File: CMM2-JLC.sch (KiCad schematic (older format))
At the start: 61 parts, among them J1 Nunchuck, J2 VGA, J3 EXTERNAL I/O, U1 STM32H743IITx, U2 MT48LC16M16A2P

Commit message: Add USB-UART, power, microSD
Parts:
- added C? (x6): 100n, Capacitor_SMD:C_0402_1005Metric, symbol Device:C
- added C? (x2): 1u, Capacitor_SMD:C_0402_1005Metric, symbol Device:C
- added C?: 4.7u, Capacitor_SMD:C_0402_1005Metric, symbol Device:C
- added C?: 10u, Capacitor_SMD:C_0603_1608Metric, symbol Device:C
- added C?: 22u, Capacitor_SMD:C_0603_1608Metric, symbol Device:C
- added J?: USB_C_Receptacle_USB2.0, symbol Connector:USB_C_Receptacle_USB2.0
- added J?: Micro_SD_Card_Det, CMM2-JLC:HOAUC_HYC77-TF09-200, symbol Connector:Micro_SD_Card_Det
- added R? (x2): 5.1k, Resistor_SMD:R_0402_1005Metric, symbol Device:R
- added R?: 4.7k, Resistor_SMD:R_0402_1005Metric, symbol Device:R
- added R?: 120R, Resistor_SMD:R_0603_1608Metric, symbol Device:R
- added R?: 10R, Resistor_SMD:R_0402_1005Metric, symbol Device:R
- added U?: SRV05-4, Package_TO_SOT_SMD:SOT-23-6, symbol Power_Protection:SRV05-4
- added U?: CP2102N-A01-GQFN28, Package_DFN_QFN:QFN-28-1EP_5x5mm_P0.5mm_EP3.35x3.35mm, symbol Interface_USB:CP2102N-A01-GQFN28
- added U?: AMS1117-3.3, Package_TO_SOT_SMD:SOT-223-3_TabPin2, symbol Regulator_Linear:AMS1117-3.3
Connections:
- net PH12 is gone; now on net GND: U1.89 (PH12)
- net +3V3: now also C?.1, C?.1, C?.1, C?.1, J?.4 (VDD), R?.1, U?.2 (VO)
- net +5V: now also C?.1, C?.1, C?.1, C?.1, J?.A4 (VBUS), J?.A9 (VBUS), J?.B4 (VBUS), J?.B9 (VBUS), U?.3 (VI), U?.5 (VP), U?.7 (REGIN), U?.8 (VBUS)
- net GND: now also C?.2, C?.2, C?.2, C?.2, C?.2, C?.2, C?.2, C?.2, C?.2, C?.2, C?.2, J?.11 (SHIELD), J?.6 (VSS), J?.9 (DET_B), J?.A1 (GND), J?.A12 (GND), J?.B1 (GND), J?.B12 (GND), J?.S1 (SHIELD), R?.1, R?.2, U?.1 (GND), U?.2 (VN), U?.29 (GND), U?.3 (GND)
- net PA11: now also U?.6 (IO4)
- net PA12: now also U?.4 (IO3)
- net PC10: now also J?.5 (CLK)
- net PC11: now also J?.7 (DAT0)
- net PC12: now also J?.3 (CMD)
- net PD2: now also J?.2 (DAT3/CD)
- net PD3: now also J?.10 (DET_A)
- net at U1.38 (VREF+): now also C?.1, R?.2
- new net: J?.A5 (CC1), R?.2
- new net: J?.B5 (CC2), R?.1
- new net: R?.2, U?.26 (TXD)
- new net: C?.1, C?.1, R?.2, U?.6 (VDD)
- new net: R?.1, U?.9 (~RSTb)
- new net PA10: R?.1
- new net PA9: U?.25 (RXD)
- new net USB_C_DM: J?.A7 (D-), J?.B7 (D-), U?.1 (IO1), U?.5 (D-)
- new net USB_C_DP: J?.A6 (D+), J?.B6 (D+), U?.3 (IO2), U?.4 (D+)
- no-connect marks 5 -> 27
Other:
- note added: "FIXME: SWD Headers"
- note added: "POWER"
- note added: "USB ESD Protection"
- note added: "USB UART"
- note added: "Write Protect\n(not present on microSD)"
- note added: "microSD"
- moved on the sheet: C1, C2, C3, C4, C5, J?

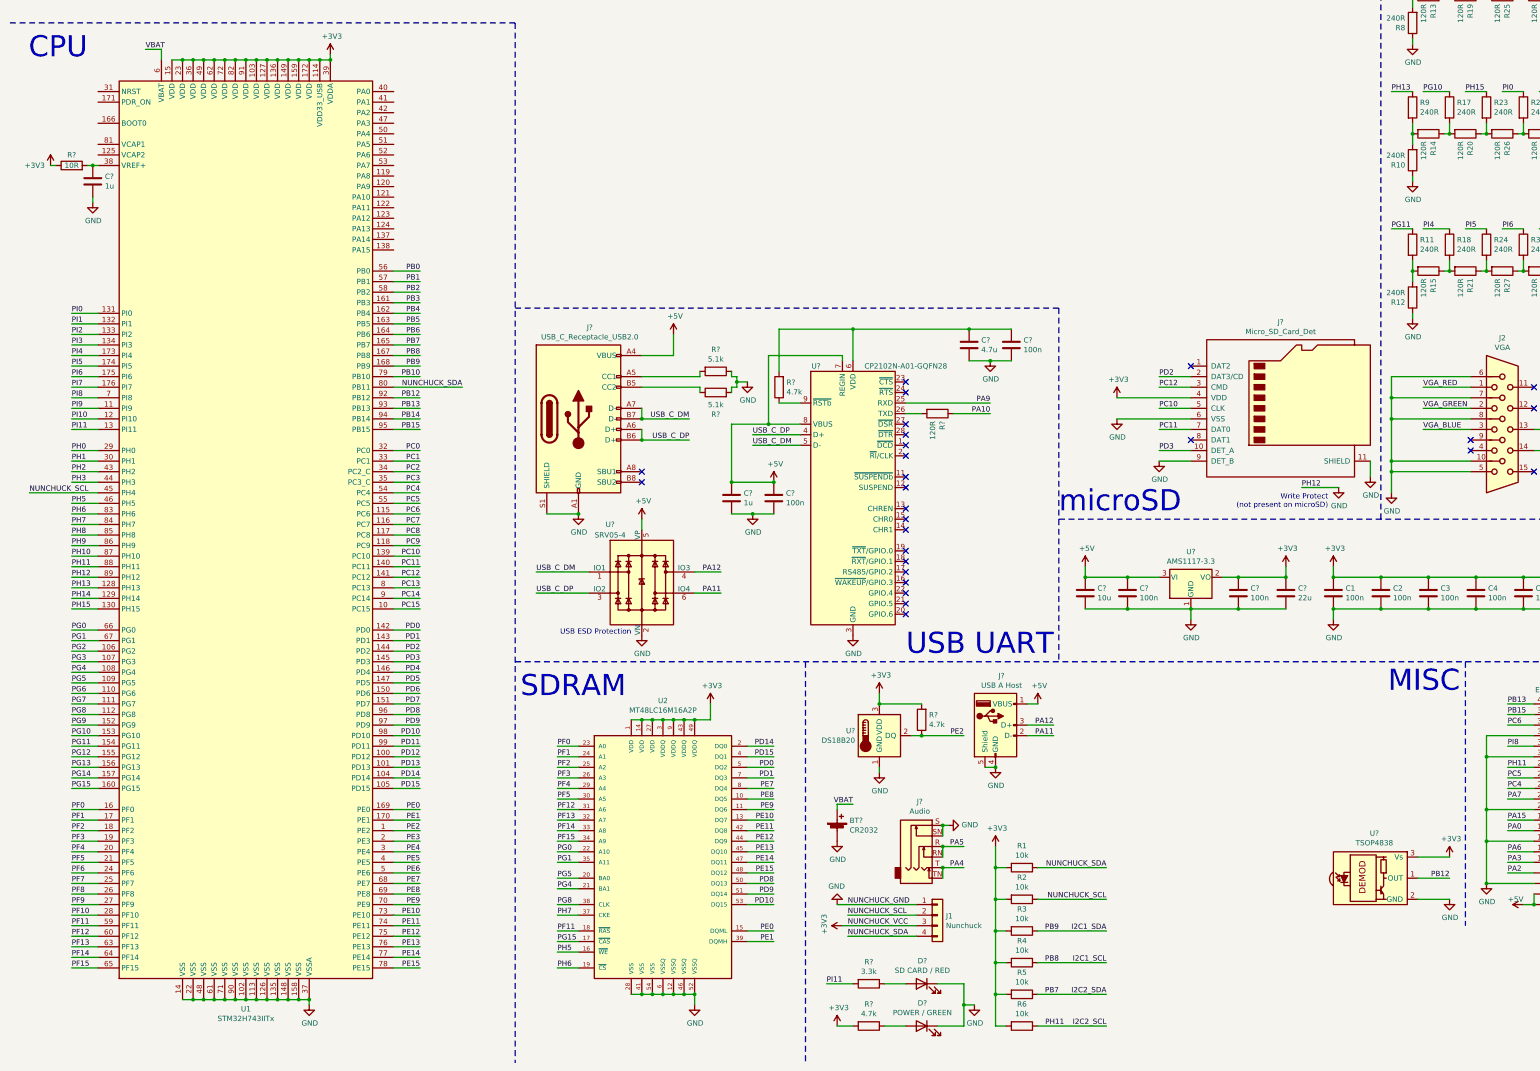
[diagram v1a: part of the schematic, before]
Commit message: Add bootstrap circuitry
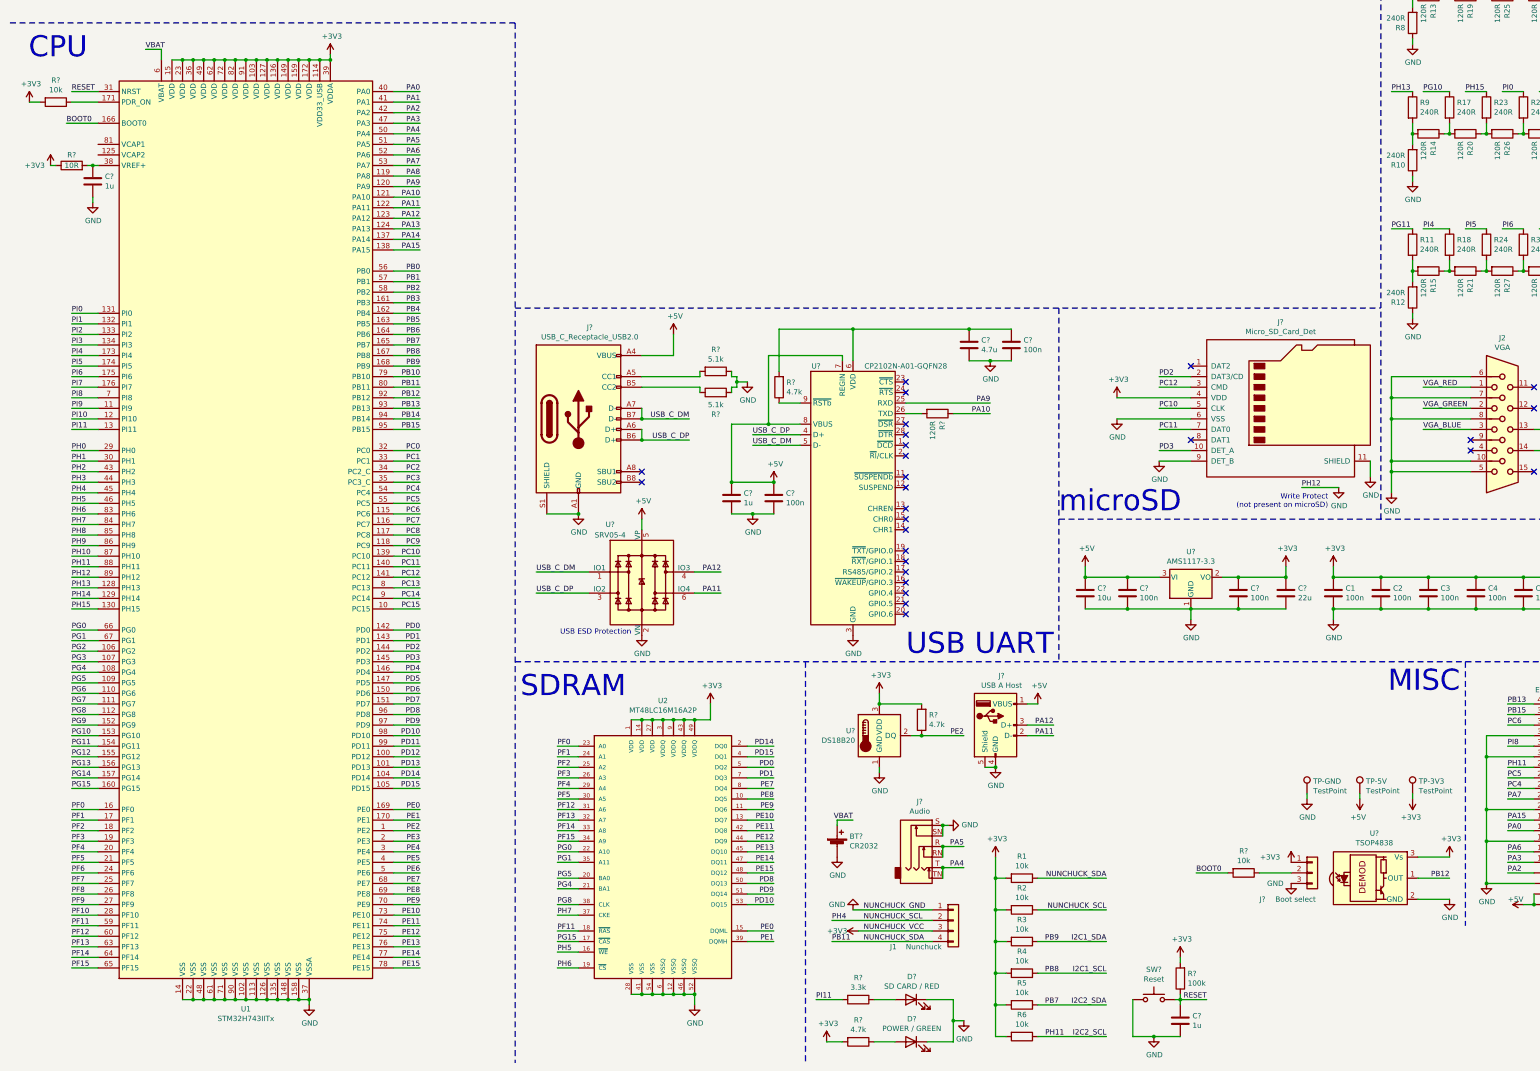
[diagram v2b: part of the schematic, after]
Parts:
- added C?: 1u, Capacitor_SMD:C_0402_1005Metric, symbol Device:C
- added J?: Boot select, Connector_PinHeader_2.54mm:PinHeader_1x03_P2.54mm_Vertical, symbol Connector_Generic:Conn_01x03
- added R?: 100k, Resistor_SMD:R_0402_1005Metric, symbol Device:R
- added R? (x2): 10k, Resistor_SMD:R_0402_1005Metric, symbol Device:R
- added SW?: Reset, CMM2-JLC:TS-1187A-X-X-X, symbol Switch:SW_Push
- added TP-3V3, TP-5V, TP-GND: TestPoint, TestPoint:TestPoint_Pad_2.0x2.0mm, symbol Connector:TestPoint
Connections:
- net +3V3: now also J?.1 (Pin_1), R?.2, R?.2, TP-3V3.1
- net +5V: now also TP-5V.1
- net GND: now also C?.2, J?.3 (Pin_3), SW?.1, TP-GND.1
- net PA0: now also U1.40 (PA0)
- net PA1: now also U1.41 (PA1)
- net PA10: now also U1.121 (PA10)
- net PA11: now also U1.122 (PA11)
- net PA12: now also U1.123 (PA12)
- net PA15: now also U1.138 (PA15)
- net PA2: now also U1.42 (PA2)
- net PA3: now also U1.47 (PA3)
- net PA4: now also U1.50 (PA4)
- net PA5: now also U1.51 (PA5)
- net PA6: now also U1.52 (PA6)
- net PA7: now also U1.53 (PA7)
- net PA9: now also U1.120 (PA9)
- net PA8: now reaches U1.119 (PA8)
- net PA13: now reaches U1.124 (PA13)
- net PA14: now reaches U1.137 (PA14)
- net BOOT0: now reaches U1.166 (BOOT0)
- net BOOT0: now also R?.2
- net at U1.171 (PDR_ON): now also R?.1
- net RESET: now reaches U1.31 (NRST)
- net RESET: now also C?.1, R?.1, SW?.2
- new net: J?.2 (Pin_2), R?.1
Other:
- moved on the sheet: BT?, D?, J1, R1, R2, R3, R4, R5, R6, R?

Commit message: Add footprints and crystals
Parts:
- added C10, C9: 6p, Capacitor_SMD:C_0402_1005Metric, symbol Device:C
- added C11, C12: 20p, Capacitor_SMD:C_0402_1005Metric, symbol Device:C
- added C6, C7: 2.2u, Capacitor_SMD:C_0603_1608Metric, symbol Device:C
- added J7: SWD, Connector_PinHeader_2.54mm:PinHeader_1x05_P2.54mm_Vertical, symbol Connector:Conn_01x05_Male
- added Y1: 32.768 kHz, Crystal:Crystal_SMD_3215-2Pin_3.2x1.5mm, symbol Device:Crystal
- added Y2: 8 MHz, Crystal:Crystal_SMD_5032-2Pin_5.0x3.2mm, symbol Device:Crystal
- J2: footprint (none) -> Connector_Dsub:DSUB-15-HD_Male_Horizontal_P2.29x1.98mm_EdgePinOffset8.35mm_Housed_MountingHolesOffset10.89mm
- J3: footprint (none) -> Connector_IDC:IDC-Header_2x20_P2.54mm_Vertical
- J4: renamed from J?; footprint (none) -> Connector_USB:USB_C_Receptacle_Palconn_UTC16-G
- J6: renamed from J?; footprint (none) -> Connector_USB:USB_A_Molex_67643_Horizontal
- U4: renamed from U?; LCSC (none) -> C6568
- gave numbers to parts that had none: 34
- renumbered TP-5V to TP-5V1, TP-GND to TP-GND1
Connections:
- net +3V3: now also J7.1 (Pin_1)
- net GND: now also C10.2, C11.1, C12.2, C6.2, C7.1, C9.1, J7.5 (Pin_5)
- net PA13: now also J7.3 (Pin_3)
- net PA14: now also J7.4 (Pin_4)
- net PC14: now also C9.2, Y1.1
- net PC15: now also C10.1, Y1.2
- net PH0: now also C11.2, Y2.1
- net PH1: now also C12.1, Y2.2
- net RESET: now also J7.2 (Pin_2)
- net at U1.125 (VCAP2): now also C7.2
- net at U1.81 (VCAP1): now also C6.1
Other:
- note added: "CLOCK"
- note removed: "FIXME: SWD Headers"
- moved on the sheet: C8, J6, J9, R42, R43, R52, TP-3V3, TP-5V1, TP-GND1, U1

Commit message: first component routing
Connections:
- net PA11 renamed USB_HOST_D-
- net USB_HOST_D-: now also U3.4 (IO3); no longer U3.6 (IO4)
- net PA12 renamed USB_HOST_D+
- net USB_HOST_D+: now also U3.6 (IO4); no longer U3.4 (IO3)
- net USB_C_DM renamed USB_C_D-
- net USB_C_DP renamed USB_C_D+
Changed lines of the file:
@@
 	1    0    0    -1
 $EndComp
-Text Label 10350 8150 2    50   ~ 0
-PA11
-Text Label 10350 8050 2    50   ~ 0
-PA12
-Wire Wire Line
-	10100 8050 10350 8050
-Wire Wire Line
-	10350 8150 10100 8150
+Text Label 10700 8150 2    50   ~ 0
+USB_HOST_D-
+Text Label 10700 8050 2    50   ~ 0
+USB_HOST_D+
 Wire Wire Line
 	9700 8450 9800 8450
@@
 	6400 6100 6400 6200
 Text Label 6850 5350 2    50   ~ 0
-USB_C_DP
+USB_C_D+
 Text Label 6850 5150 2    50   ~ 0
-USB_C_DM
+USB_C_D-
 Text Label 5400 6600 0    50   ~ 0
-USB_C_DM
+USB_C_D-
 Text Label 5400 6800 0    50   ~ 0
-USB_C_DP
+USB_C_D+
 Wire Wire Line
 	5400 6600 5900 6600
@@
 NoConn ~ 6400 5650
 NoConn ~ 6400 5750
-Text Label 7150 6600 2    50   ~ 0
-PA12
-Text Label 7150 6800 2    50   ~ 0
-PA11
-Wire Wire Line
-	6900 6600 7150 6600
-Wire Wire Line
-	7150 6800 6900 6800
+Text Label 7500 6800 2    50   ~ 0
+USB_HOST_D+
+Text Label 7500 6600 2    50   ~ 0
+USB_HOST_D-
 $Comp
 L power:GND #PWR0135
@@
 Text Notes 6300 7200 2    50   ~ 0
 USB ESD Protection
-$Comp
-L Interface_USB:CP2102N-A01-GQFN28 U4
-U 1 1 62161A24
-P 8400 5900
-F 0 "U4" H 8050 7150 50  0000 C CNN
-F 1 "CP2102N-A01-GQFN28" H 8900 7150 50  0000 C CNN
-F 2 "Package_DFN_QFN:QFN-28-1EP_5x5mm_P0.5mm_EP3.35x3.35mm" H 8850 4700 50  0001 L CNN
-F 3 "https://www.silabs.com/documents/public/data-sheets/cp2102n-datasheet.pdf" H 8450 5150 50  0001 C CNN
-F 4 "C6568" H 8400 5900 50  0001 C CNN "LCSC"
-	1    8400 5900
-	1    0    0    -1
-$EndComp
 NoConn ~ 8900 7000
 NoConn ~ 8900 6900
@@
 Connection ~ 9500 4300
 Text Label 7450 5400 0    50   ~ 0
-USB_C_DM
+USB_C_D-
 Text Label 7450 5300 0    50   ~ 0
-USB_C_DP
+USB_C_D+
 Wire Wire Line
 	7900 5300 7450 5300
@@
 	11000 6950 10600 6950
 Connection ~ 11600 6950
-Wire Wire Line
-	11600 6950 11000 6950
 Connection ~ 12050 6950
 Wire Wire Line
@@
 	1    0    0    -1
 $EndComp
-Wire Wire Line
-	11600 4950 10900 4950
 $Comp
 L power:GND #PWR0146
@@
 	1    0    0    -1
 $EndComp
-Wire Wire Line
-	11600 5150 10900 5150
 Text Label 11300 4750 0    50   ~ 0
 PD2
@@
 Wire Wire Line
 	12650 5800 13000 5800
-Wire Wire Line
-	11300 4750 11600 4750
-Wire Wire Line
-	11600 4850 11300 4850
-Wire Wire Line
-	11300 5050 11600 5050
-Wire Wire Line
-	11600 5250 11300 5250
 NoConn ~ 11600 4650
 NoConn ~ 11600 5350
 Text Label 11300 5450 0    50   ~ 0
 PD3
-Wire Wire Line
-	11300 5450 11600 5450
 $Comp
 L power:GND #PWR0148
@@
 Text Label 4800 3150 2    50   ~ 0
 PA10
-Text Label 4800 3250 2    50   ~ 0
-PA11
-Text Label 4800 3350 2    50   ~ 0
-PA12
+Text Label 5150 3250 2    50   ~ 0
+USB_HOST_D-
+Text Label 5150 3350 2    50   ~ 0
+USB_HOST_D+
 Text Label 4800 3450 2    50   ~ 0
 PA13
@@
 Wire Wire Line
 	4800 3150 4550 3150
-Wire Wire Line
-	4800 3250 4550 3250
-Wire Wire Line
-	4550 3350 4800 3350
 Wire Wire Line
 	4800 3450 4550 3450
@@
 Wire Notes Line
 	10350 7450 10350 4100
+Wire Wire Line
+	11600 5250 11300 5250
+Wire Wire Line
+	11600 5150 10900 5150
+Wire Wire Line
+	11300 5050 11600 5050
+Wire Wire Line
+	11600 4950 10900 4950
+Wire Wire Line
+	11600 4850 11300 4850
+Wire Wire Line
+	11300 4750 11600 4750
+Wire Wire Line
+	11600 6950 11000 6950
+Wire Wire Line
+	11300 5450 11600 5450
+$Comp
+L Interface_USB:CP2102N-A01-GQFN28 U4
+U 1 1 62161A24
+P 8400 5900
+F 0 "U4" H 8050 7150 50  0000 C CNN
+F 1 "CP2102N-A01-GQFN28" H 8900 7150 50  0000 C CNN
+F 2 "Package_DFN_QFN:QFN-28-1EP_5x5mm_P0.5mm_EP3.35x3.35mm" H 8850 4700 50  0001 L CNN
+F 3 "https://www.silabs.com/documents/public/data-sheets/cp2102n-datasheet.pdf" H 8450 5150 50  0001 C CNN
+F 4 "C6568" H 8400 5900 50  0001 C CNN "LCSC"
+	1    8400 5900
+	1    0    0    -1
+$EndComp
+Wire Wire Line
+	10100 8050 10700 8050
+Wire Wire Line
+	4550 3250 5150 3250
+Wire Wire Line
+	4550 3350 5150 3350
+Wire Wire Line
+	6900 6600 7500 6600
+Wire Wire Line
+	6900 6800 7500 6800
+Wire Wire Line
+	10100 8150 10700 8150
 $EndSCHEMATC

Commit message: Replace VGA connector
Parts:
- J2: footprint Connector_Dsub:DSUB-15-HD_Male_Horizontal_P2.29x1.98mm_EdgePinOffset8.35mm_Housed_MountingHolesOffset10.89mm -> Connector_Dsub:DSUB-15-HD_Female_Horizontal_P2.29x1.98mm_EdgePinOffset8.35mm_Housed_MountingHolesOffset10.89mm
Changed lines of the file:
@@
 F 0 "J2" H 14550 6117 50  0000 C CNN
 F 1 "VGA" H 14550 6026 50  0000 C CNN
-F 2 "Connector_Dsub:DSUB-15-HD_Male_Horizontal_P2.29x1.98mm_EdgePinOffset8.35mm_Housed_MountingHolesOffset10.89mm" H 13600 5650 50  0001 C CNN
+F 2 "Connector_Dsub:DSUB-15-HD_Female_Horizontal_P2.29x1.98mm_EdgePinOffset8.35mm_Housed_MountingHolesOffset10.89mm" H 13600 5650 50  0001 C CNN
 F 3 " ~" H 13600 5650 50  0001 C CNN
 	1    14550 5250
